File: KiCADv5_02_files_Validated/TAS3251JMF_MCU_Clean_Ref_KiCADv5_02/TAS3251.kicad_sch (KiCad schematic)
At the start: 133 parts, among them J1 Oscill sync, J10 Conn_01x03, J11 Conn_01x06, J12 Conn_02x03_Odd_Even, J13 Conn_01x04, J15 Conn_02x05, J16 Conn_01x03, J17 Conn_01x10, J19 Conn_01x04, J2 Freq Adjust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

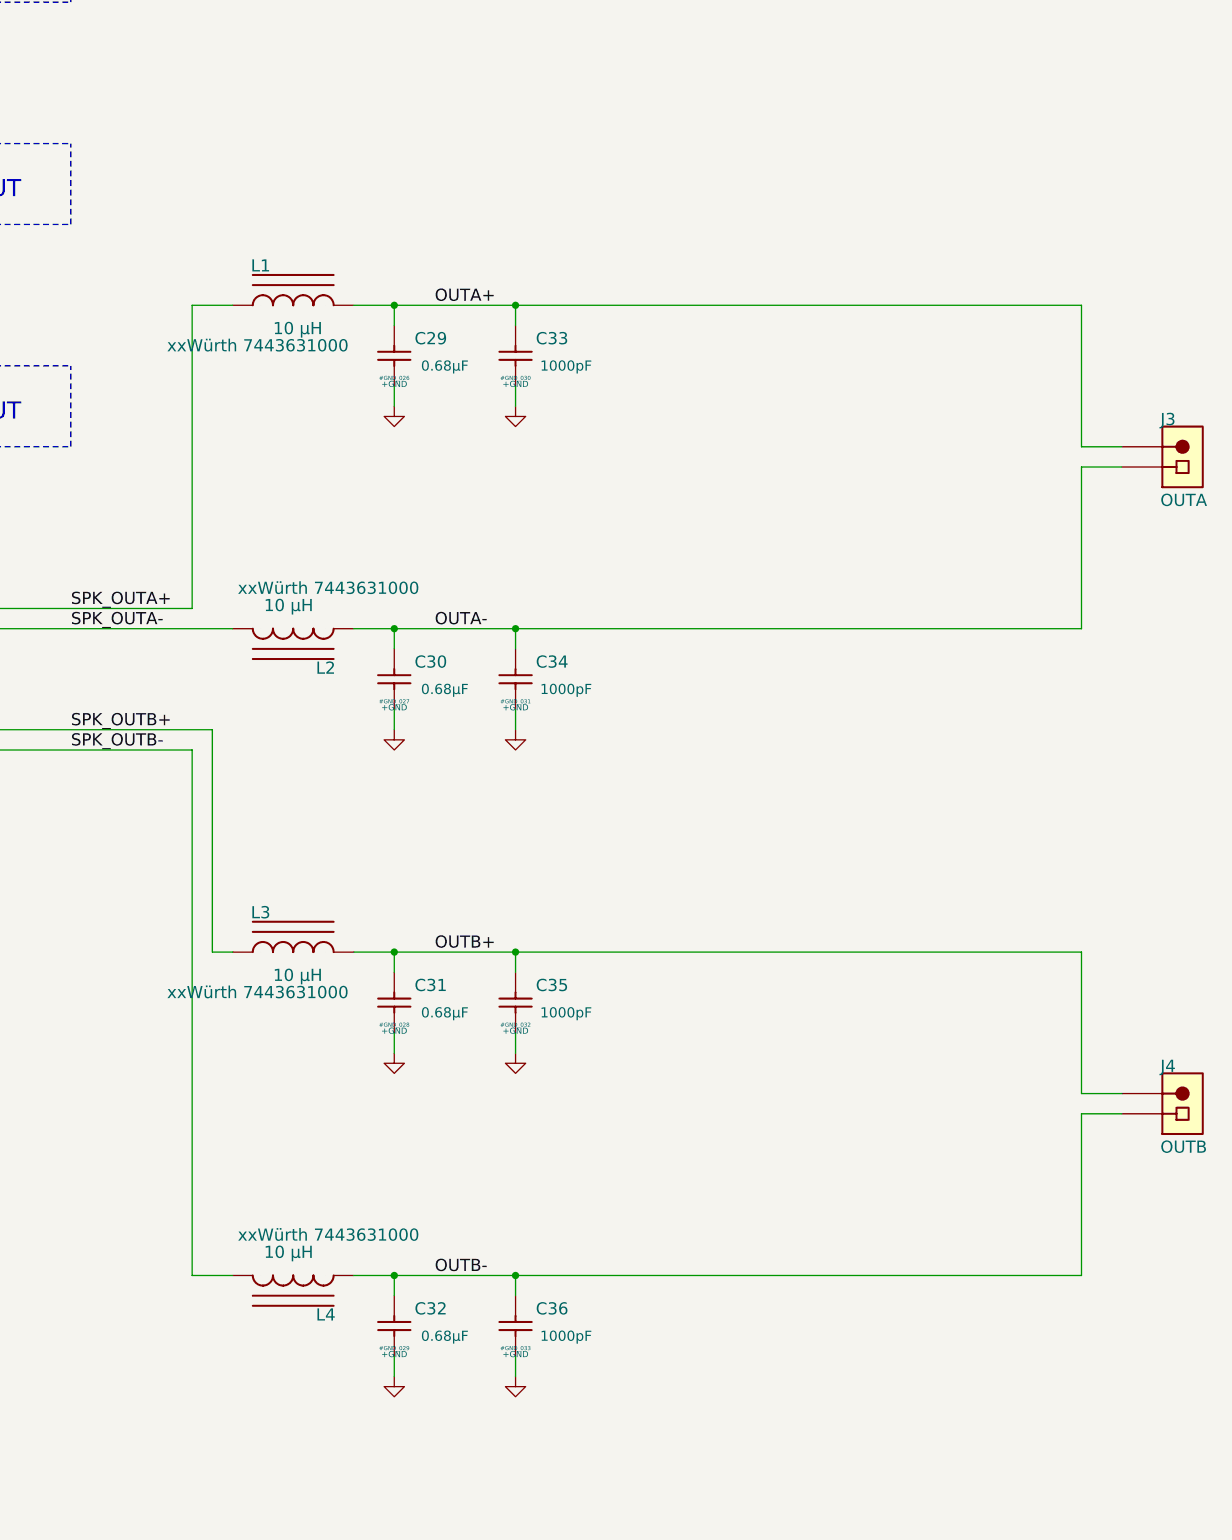
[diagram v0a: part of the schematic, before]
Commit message: Adding development placeholders. Moving uC SCH to separate sheet.
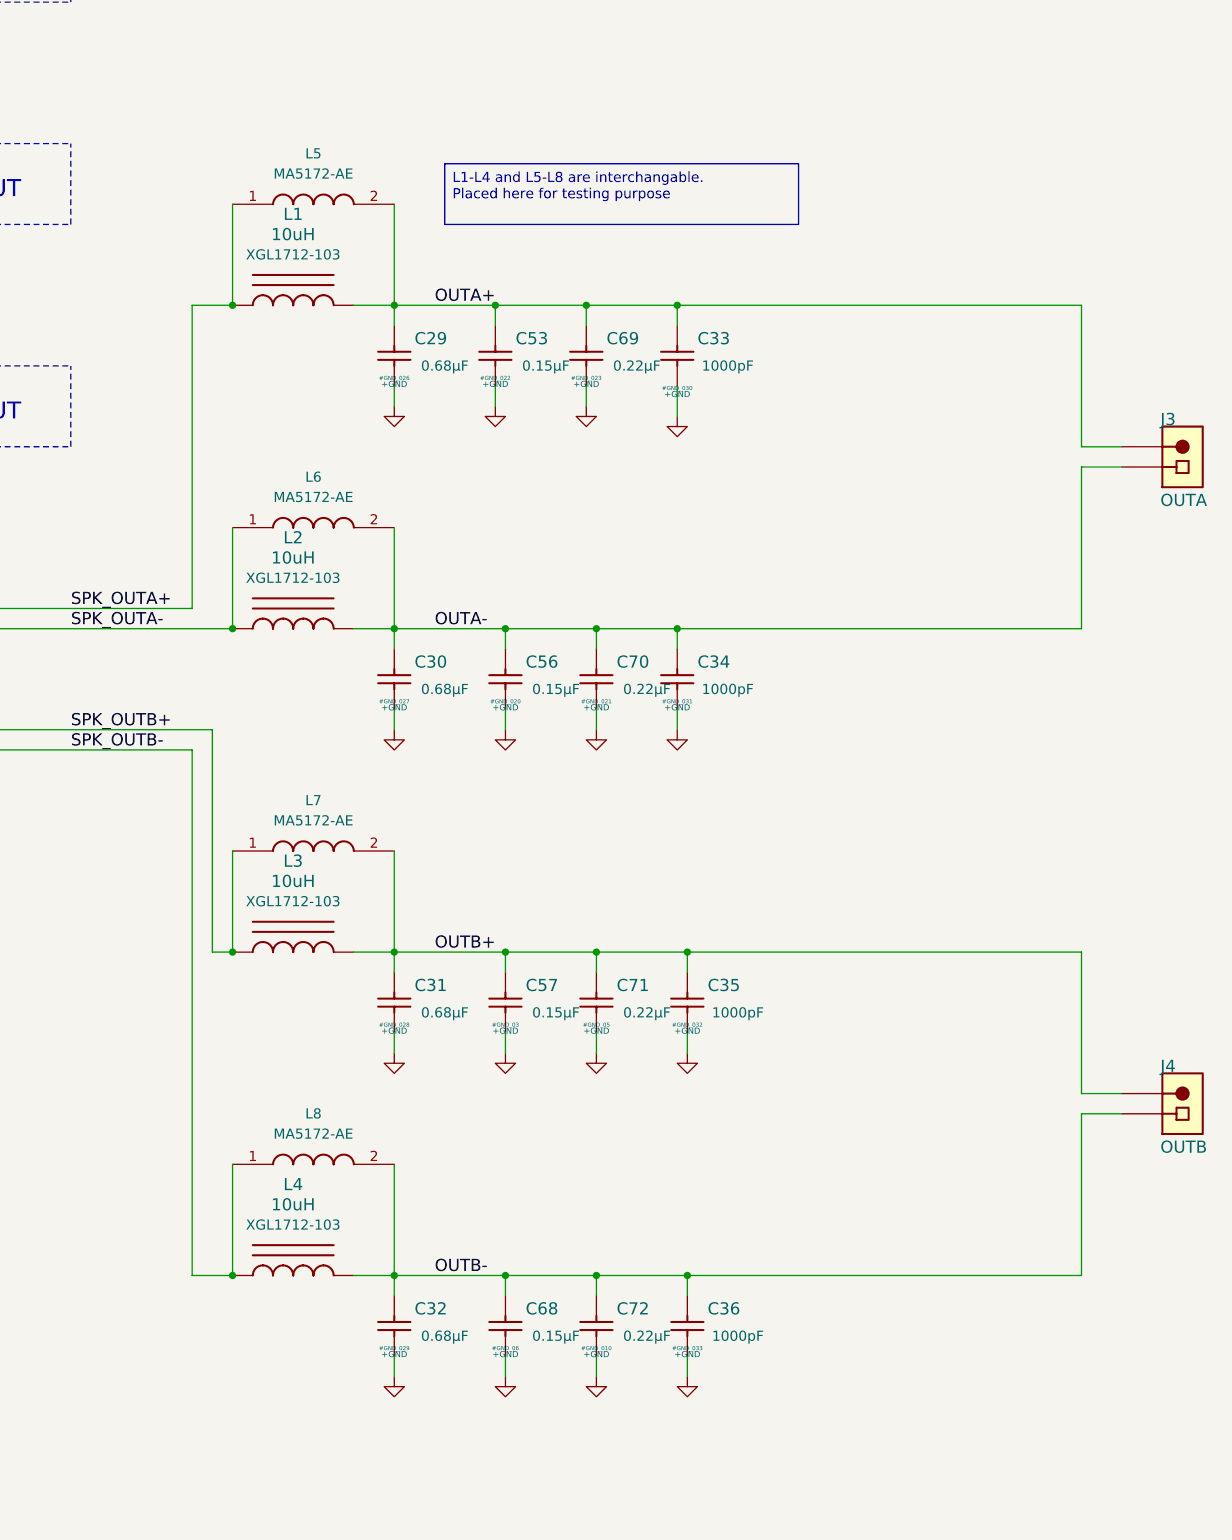
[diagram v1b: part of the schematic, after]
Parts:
- removed L1, L2, L3, L4: 10 µH, SamacSys_Parts:WE-HCF_201322, symbol AAP090A_TAS3251DKQ-IO-SchDoc-rescue:MA5173-AE
- added C53, C56, C57, C68: 0.15µF, Capacitor_THT:C_Rect_L18.0mm_W6.0mm_P15.00mm_FKS3_FKP3, symbol AAP090A_TAS3251DKQ-IO-SchDoc-rescue:B32652A3684J
- added C69, C70, C71, C72: 0.22µF, Capacitor_THT:C_Rect_L18.0mm_W6.0mm_P15.00mm_FKS3_FKP3, symbol AAP090A_TAS3251DKQ-IO-SchDoc-rescue:B32652A3684J
- added L1, L2, L3, L4: 10uH, TAS3251:L_Coilcraft_XGL1712-103, symbol TAS3251_project:Coilcraft_XGL1712-103MED
- added L5, L6, L7, L8: MA5172-AE, MA5172:MA5172AE, symbol MA5172-AE:MA5172-AE
- C25, C26, C27, C28: footprint Capacitor_THT:CP_Radial_D5.0mm_P2.00mm -> Capacitor_SMD:C_1210_3225Metric; Manufacturer ELNA -> Murata; PartNumber RFS-16V100ME3#5 -> GRJ32ER71H106KE11K; Value2 x16V -> x50V
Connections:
- net +GND: now also C53.2, C56.2, C57.2, C68.2, C69.2, C70.2, C71.2, C72.2
- net OUTA+: now also C53.1, C69.1, L1.2, L5.2
- net OUTA-: now also C56.1, C70.1, L2.2, L6.2
- net OUTB+: now also C57.1, C71.1, L3.2, L7.2
- net OUTB-: now also C68.1, C72.1, L4.2, L8.2
- net SPK_OUTA+: now also L1.1, L5.1
- net SPK_OUTA-: now also L2.1, L6.1
- net SPK_OUTB+: now also L3.1, L7.1
- net SPK_OUTB-: now also L4.1, L8.1
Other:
- moved on the sheet: C33, C34, C35, C36

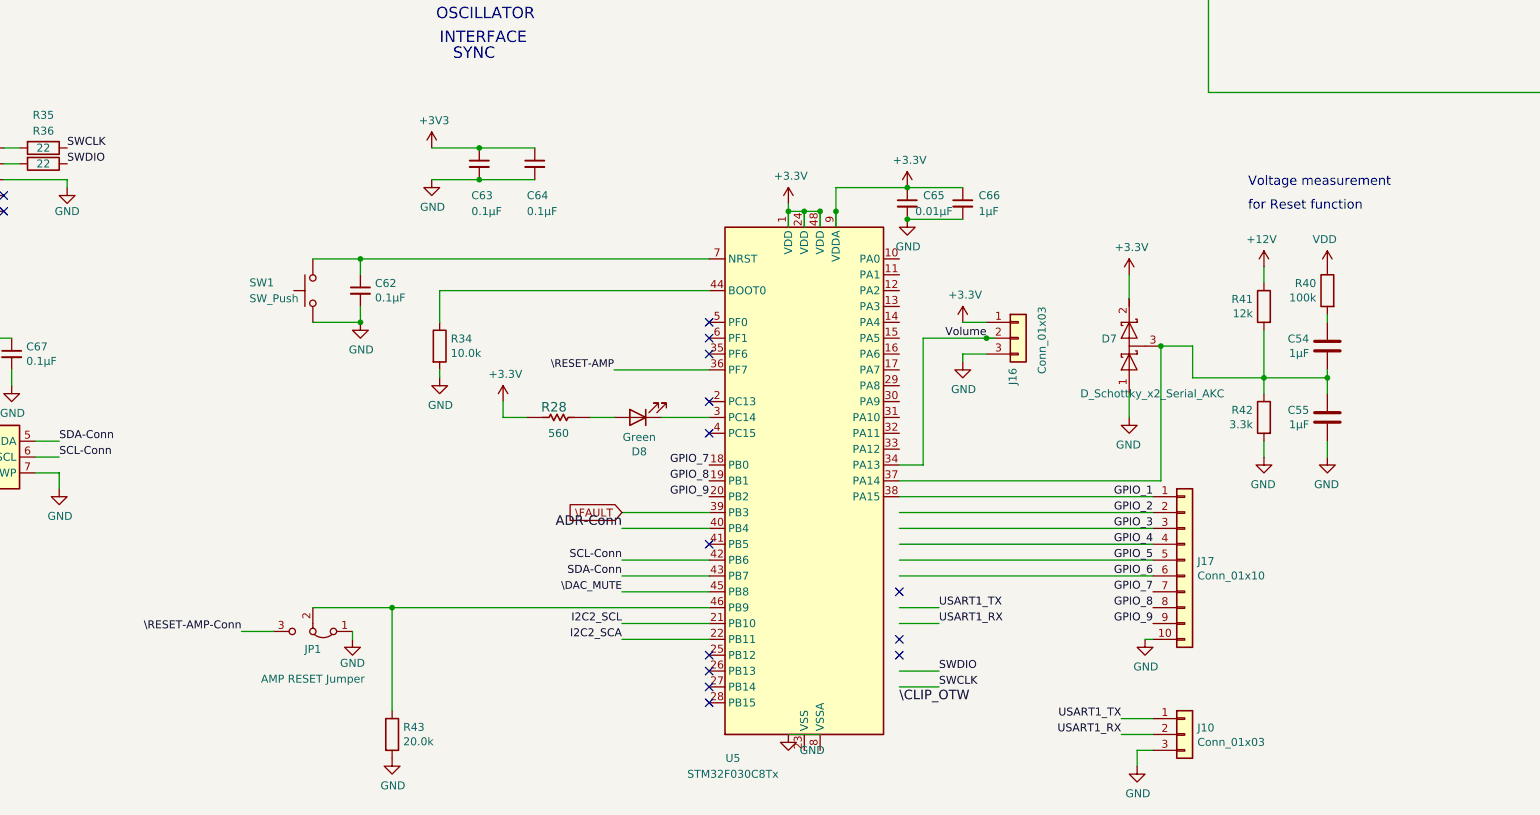
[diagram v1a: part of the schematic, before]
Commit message: Separating SCHs
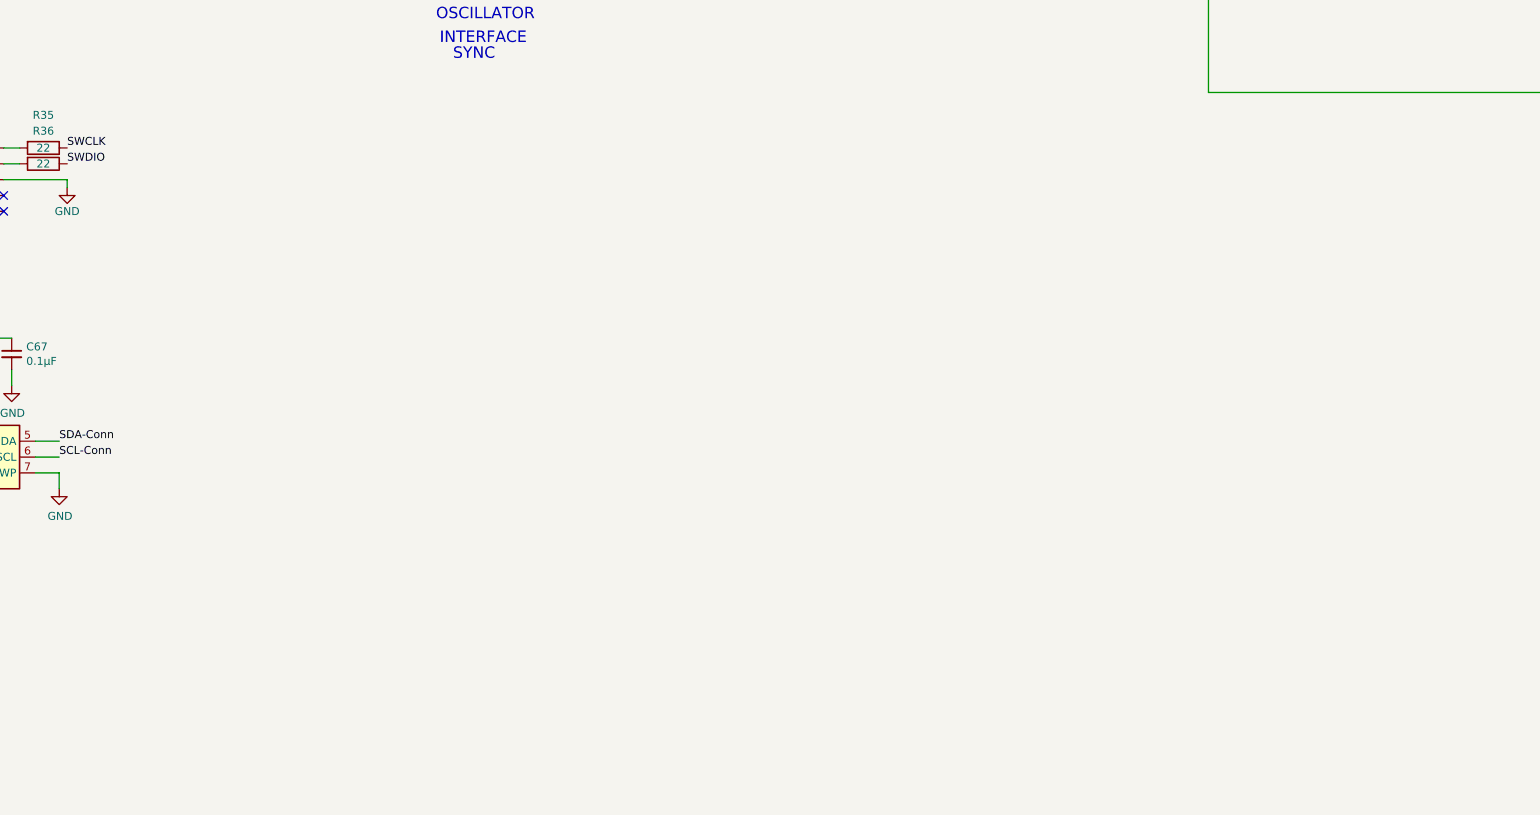
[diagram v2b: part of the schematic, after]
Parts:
- removed C54, C55: 1µF, Capacitor_SMD:C_0805_2012Metric_Pad1.15x1.40mm_HandSolder, symbol Device:C
- removed C62, C63, C64: 0.1µF, Capacitor_SMD:C_0805_2012Metric_Pad1.15x1.40mm_HandSolder, symbol Device:C_Small
- removed C65: 0.01µF, Capacitor_SMD:C_0805_2012Metric_Pad1.15x1.40mm_HandSolder, symbol Device:C_Small
- removed C66: 1µF, Capacitor_SMD:C_0805_2012Metric_Pad1.15x1.40mm_HandSolder, symbol Device:C_Small
- removed D7: D_Schottky_x2_Serial_AKC, Package_TO_SOT_SMD:SOT-23, symbol Device:D_Schottky_x2_Serial_AKC
- removed D8: Green, LED_SMD:LED_0603_1608Metric, symbol Device:LED
- removed J10, J16: Conn_01x03, Connector_PinHeader_2.54mm:PinHeader_1x03_P2.54mm_Vertical, symbol Connector_Generic:Conn_01x03
- removed J17: Conn_01x10, Connector_PinHeader_2.54mm:PinHeader_1x10_P2.54mm_Vertical, symbol Connector_Generic:Conn_01x10
- removed JP1: AMP RESET Jumper, Connector_PinHeader_2.54mm:PinHeader_1x03_P2.54mm_Vertical, symbol Jumper:Jumper_3_Bridged12
- removed R28: 560, Resistor_SMD:R_0603_1608Metric, symbol AAP090A_TAS3251DKQ-IO-SchDoc-rescue:RC0603JR-07560RL
- removed R34: 10.0k, Resistor_SMD:R_0805_2012Metric_Pad1.15x1.40mm_HandSolder, symbol Device:R
- removed R40: 100k, Resistor_SMD:R_0805_2012Metric_Pad1.15x1.40mm_HandSolder, symbol Device:R
- removed R41: 12k, Resistor_SMD:R_0805_2012Metric_Pad1.15x1.40mm_HandSolder, symbol Device:R
- removed R42: 3.3k, Resistor_SMD:R_0805_2012Metric_Pad1.15x1.40mm_HandSolder, symbol Device:R
- removed R43: 20.0k, Resistor_SMD:R_0805_2012Metric_Pad1.15x1.40mm_HandSolder, symbol Device:R
- removed SW1: SW_Push, Button_Switch_SMD:SW_SPST_TL3342, symbol Switch:SW_Push
- removed U5: STM32F030C8Tx, Package_QFP:LQFP-48_7x7mm_P0.5mm, symbol MCU_ST_STM32F0:STM32F030C8Tx
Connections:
- no-connect marks 18 -> 5
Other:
- note removed: "Voltage measurement"
- note removed: "for Reset function"

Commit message: adding components
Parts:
- removed C67: 0.1µF, Capacitor_SMD:C_0805_2012Metric_Pad1.15x1.40mm_HandSolder, symbol Device:C_Small
- removed D6: Green, LED_SMD:LED_0805_2012Metric_Pad1.15x1.40mm_HandSolder, symbol Device:LED
- removed J15: Conn_02x05, Connector_IDC:IDC-Header_2x05_P2.54mm_Vertical, symbol Connector_Generic:Conn_02x05_Odd_Even
- removed JP6, JP7, JP8: SolderJumper_3_Open, Jumper:SolderJumper-3_P1.3mm_Open_RoundedPad1.0x1.5mm_NumberLabels, symbol Jumper:SolderJumper_3_Open
- removed R35, R36: 22, Resistor_SMD:R_0603_1608Metric, symbol Device:R
- removed R37: 560, Resistor_SMD:R_0805_2012Metric_Pad1.15x1.40mm_HandSolder, symbol AAP090A_TAS3251DKQ-IO-SchDoc-rescue:RC0603JR-07560RL
- removed R45, R46, R47: 10.0k, Resistor_SMD:R_0603_1608Metric, symbol Device:R
- removed U4: AT24C256C, Package_SO:SOIC-8_3.9x4.9mm_P1.27mm, symbol Memory_EEPROM:24LC02
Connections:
- net \CLIP_OTW renamed \CLP_OTW
- no-connect marks 5 -> 0
